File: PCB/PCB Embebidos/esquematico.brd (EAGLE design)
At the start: 91 x 70.9 mm, 30 parts, among them IC1 LM358N, IC2 317T, T1 BT138-V

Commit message: Estuve ruteando el PCB. Creo que esta terminado, pero tendria que revisarlo menos dormido
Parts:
- moved ALIMENTACION 39.9 mm to (6.96, 58.2), turned to 180 degrees
- moved CARGA 39.4 mm to (81.1, 24.6), turned to 270 degrees
- moved R9 17.7 mm to (13.7, 23.6), turned to 270 degrees
- moved R11 17.0 mm to (17.2, 20.8), turned to 270 degrees
- moved D1 16.2 mm to (72.2, 38.1), turned to 180 degrees
- moved IC2 15.4 mm to (-3.59, 25.9)
- moved R10 14.3 mm to (35.6, 62.5), turned to 0 degrees
- moved C1 14.3 mm to (7.43, 35.5)
- moved C4 13.6 mm to (7.37, 39.4)
- moved R2 13.2 mm to (65.1, 51.4)
- moved C5 9.36 mm to (12.9, 39.4)
- moved OK2 8.81 mm to (50.5, 37.1)
- moved R6 8.81 mm to (58.8, 37.1)
- moved OK3 8.62 mm to (59.9, 46.2)
- moved R5 8.37 mm to (42.7, 37.6), turned to 90 degrees
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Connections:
- net AC-: now also AC.2, CARGA.2; no longer CARGA.1
- net GND: now also ALIMENTACION.1, OK3.2; no longer ALIMENTACION.2
- net N$4: now also CARGA.1; no longer CARGA.2
- net VCC: now also ALIMENTACION.2; no longer ALIMENTACION.1
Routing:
- net VCC: track 0.00 -> 125.6 mm
- net AC+: track 0.00 -> 72.6 mm
- net AC-: track 0.00 -> 49.9 mm
- net N$4: track 0.00 -> 44.3 mm
- net VCC_5V: track 0.00 -> 32.6 mm
- net TERMOCUPLA: track 0.00 -> 31.8 mm
- net SAL_TERMOCUPLA: track 0.00 -> 30.6 mm
- net FASE: track 0.00 -> 28.4 mm
- net SAL_PT100: track 0.00 -> 25.6 mm
- net N$8: track 0.00 -> 25.3 mm
- net N$7: track 0.00 -> 18.6 mm
- net N$3: track 0.00 -> 13.6 mm
- net N$9: track 0.00 -> 13.0 mm
- net N$5: track 0.00 -> 12.1 mm
- net N$6: track 0.00 -> 11.9 mm
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- added copper zone on layer 16, net GND
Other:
- board size 91 x 70.9 mm -> 88.3 x 65.2 mm
- board text added: "Zorzuino ®"

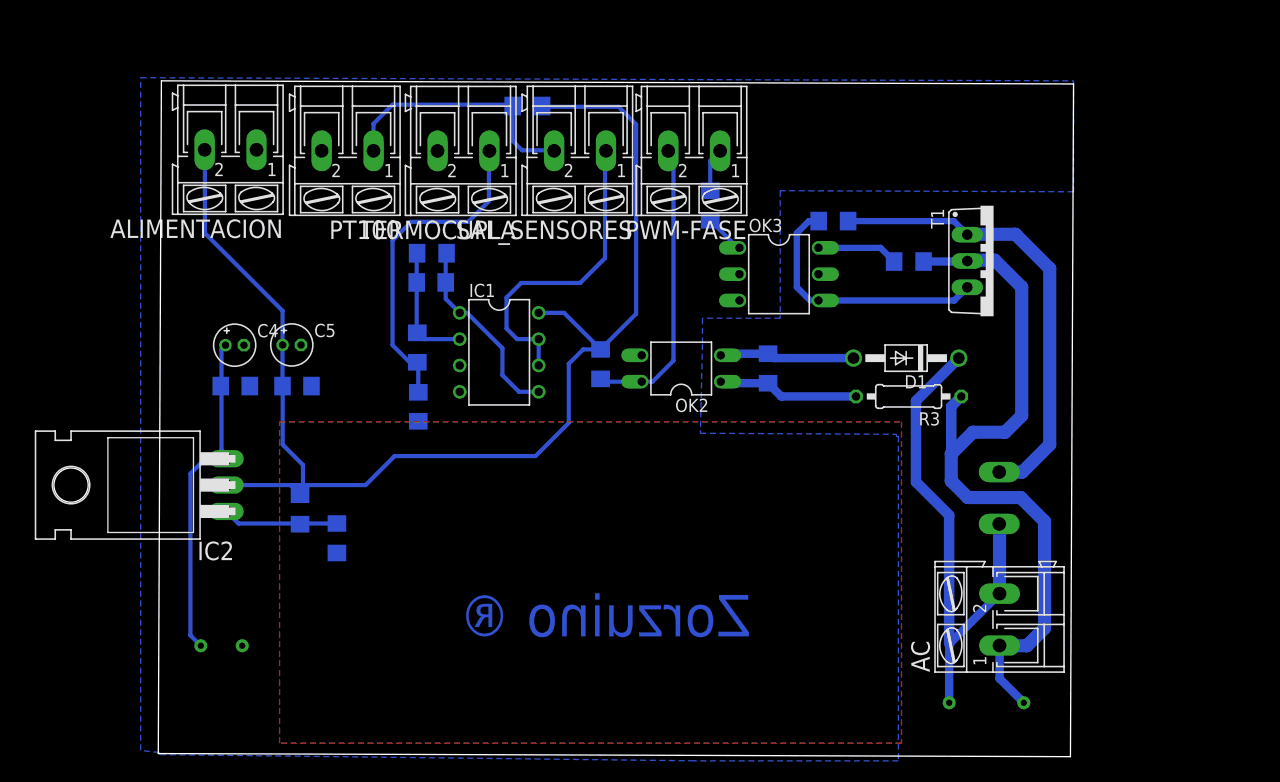
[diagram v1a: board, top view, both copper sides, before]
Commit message: Borre lo del PT100 y agrege las cosas para hacer el control del cooler. Falta ordenar un poco, ver si se puede achicar mas, y volver a rutear
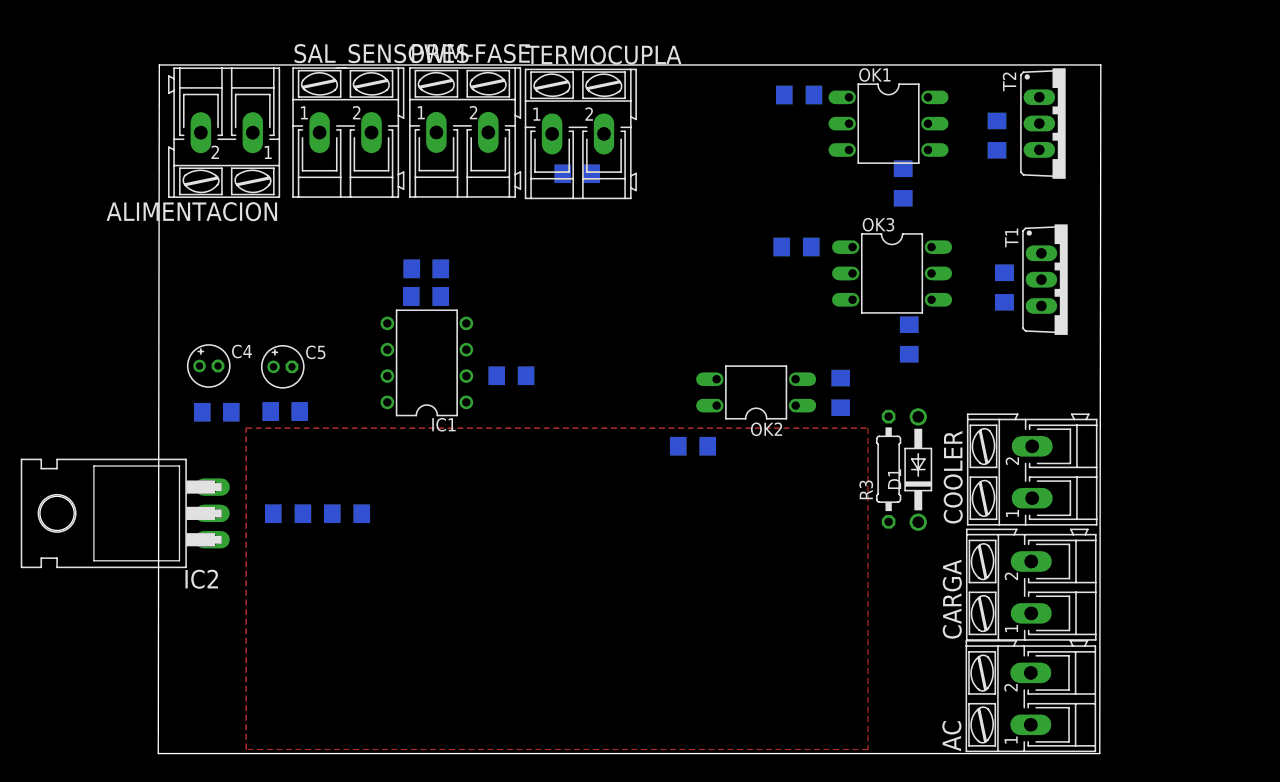
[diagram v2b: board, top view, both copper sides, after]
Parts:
- removed PT100: (no value), con-ptr500:AK300/2
- added COOLER: (no value), con-ptr500:AK300/2
- added OK1: MOC3031M, optocoupler:DIL06
- added R12, R13: 330, resistor:R1206
- added T2: BT138-V, triac:TO220BV
- R10: value 100 -> 680
- moved C6 27.2 mm to (40.4, 55.9), turned to 180 degrees
- moved R10 26.2 mm to (61.8, 63.5), turned to 180 degrees
- moved SAL_SENSORES 22.7 mm to (18.1, 59.9), turned to 0 degrees
- moved PWM-FASE 22.4 mm to (29.4, 59.9), turned to 0 degrees
- moved R2 17.7 mm to (81.6, 45.0), turned to 90 degrees
- moved R5 11.9 mm to (51.6, 29.6), turned to 0 degrees
- moved TERMOCUPLA 11.2 mm to (40.5, 59.8), turned to 0 degrees
- moved OK3 10.9 mm to (70.8, 46.3)
- moved D1 10.8 mm to (73.3, 27.4), turned to 90 degrees
- moved R8 9.47 mm to (34.1, 36.5), turned to 180 degrees
- moved R4 9.23 mm to (61.6, 48.9), turned to 180 degrees
- moved CARGA 9.14 mm to (84.2, 16.0), flipped to the top, turned to 90 degrees
- moved AC 8.22 mm to (84.2, 5.29)
- moved OK2 7.59 mm to (57.7, 34.8)
- moved R1 7.52 mm to (72.5, 40.0), turned to 270 degrees
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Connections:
- removed net SAL_PT100: PT100.1, R10.2, SAL_SENSORES.2
- new net COOLER_PIN: R10.1, SAL_SENSORES.2
- new net N$11: OK1.1, R10.2
- new net N$12: OK1.6, R12.1
- new net N$15: OK1.4, R13.1, T2.G
- new net N$17: COOLER.2, R13.2, T2.T1
- net AC+: now also R12.2, T2.T2
- net AC-: now also COOLER.1
- net GND: now also OK1.2; no longer PT100.2
- net VCC: no longer R10.1
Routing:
- net VCC: track 125.6 -> 0.00 mm
- net AC+: track 72.6 -> 0.00 mm, vias 1 -> 0
- net AC-: track 49.9 -> 0.00 mm, vias 1 -> 0
- net N$4: track 44.3 -> 0.00 mm
- net VCC_5V: track 32.6 -> 0.00 mm, vias 1 -> 0
- net TERMOCUPLA: track 31.8 -> 0.00 mm
- net SAL_TERMOCUPLA: track 30.6 -> 0.00 mm
- net FASE: track 28.4 -> 0.00 mm
- net SAL_PT100: track 25.6 -> 0.00 mm
- net N$8: track 25.3 -> 0.00 mm
- net N$7: track 18.6 -> 0.00 mm
- net N$3: track 13.6 -> 0.00 mm
- net N$9: track 13.0 -> 0.00 mm
- net N$5: track 12.1 -> 0.00 mm
- net N$6: track 11.9 -> 0.00 mm
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- removed copper zone on layer 16, net GND
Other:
- board size 88.3 x 65.2 mm -> 90.9 x 66.4 mm
- board text removed: "Zorzuino ®"

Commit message: El PCB esta listo para ser imprimido. Voy a comprar todos los componentes mañana y ya lo termino
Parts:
- moved R1 19.3 mm to (91.8, 39.5), turned to 180 degrees
- moved R12 15.4 mm to (87.3, 54.0), turned to 180 degrees
- moved COOLER 14.5 mm to (93.6, 16.0)
- moved CARGA 14.3 mm to (93.6, 26.9)
- moved PWM-FASE 14.2 mm to (43.5, 59.8), turned to 180 degrees
- moved OK3 11.1 mm to (81.9, 46.0)
- moved R13 11.1 mm to (92.0, 59.3)
- moved R2 11.1 mm to (92.7, 44.6)
- moved T1 11.1 mm to (98.8, 45.4)
- moved T2 11.1 mm to (98.6, 60.5)
- moved R5 10.3 mm to (61.9, 30.0)
- moved D1 9.47 mm to (82.8, 27.4)
- moved R3 9.47 mm to (79.9, 27.4)
- moved OK2 9.47 mm to (67.2, 34.8)
- moved AC 9.47 mm to (93.7, 5.29)
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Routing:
- net AC+: track 0.00 -> 134.3 mm, vias 0 -> 1
- net VCC: track 0.00 -> 101.5 mm
- net N$17: track 0.00 -> 80.1 mm
- net AC-: track 0.00 -> 63.0 mm, vias 0 -> 1
- net FASE: track 0.00 -> 51.2 mm
- net N$4: track 0.00 -> 50.3 mm
- net COOLER_PIN: track 0.00 -> 38.5 mm
- net VCC_5V: track 0.00 -> 27.0 mm, vias 0 -> 1
- net TERMOCUPLA: track 0.00 -> 25.4 mm
- net SAL_TERMOCUPLA: track 0.00 -> 24.1 mm
- net PWM: track 0.00 -> 23.6 mm
- net N$15: track 0.00 -> 17.3 mm
- net N$7: track 0.00 -> 17.0 mm
- net N$12: track 0.00 -> 16.1 mm
- net N$1: track 0.00 -> 15.8 mm, vias 0 -> 2
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- added copper zone on layer 16, net GND
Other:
- board size 90.9 x 66.4 mm -> 105.1 x 66.5 mm
- board text added: "Zorzuino ®"

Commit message: Movi unas cosas para que entren mejor los disipadores
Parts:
- moved C1 10.3 mm to (5.74, 43.2)
- moved C2 10.3 mm to (12.3, 43.2)
- moved C4 10.3 mm to (4.96, 47.6)
- moved C5 10.3 mm to (12.1, 47.6)
- moved IC2 10.3 mm to (-4.85, 33.4)
- moved R9 10.3 mm to (12.6, 33.4)
- moved R11 8.89 mm to (16.9, 31.9), turned to 270 degrees
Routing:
- net VCC: track 101.5 -> 86.7 mm
- net VCC_5V: track 27.0 -> 37.2 mm

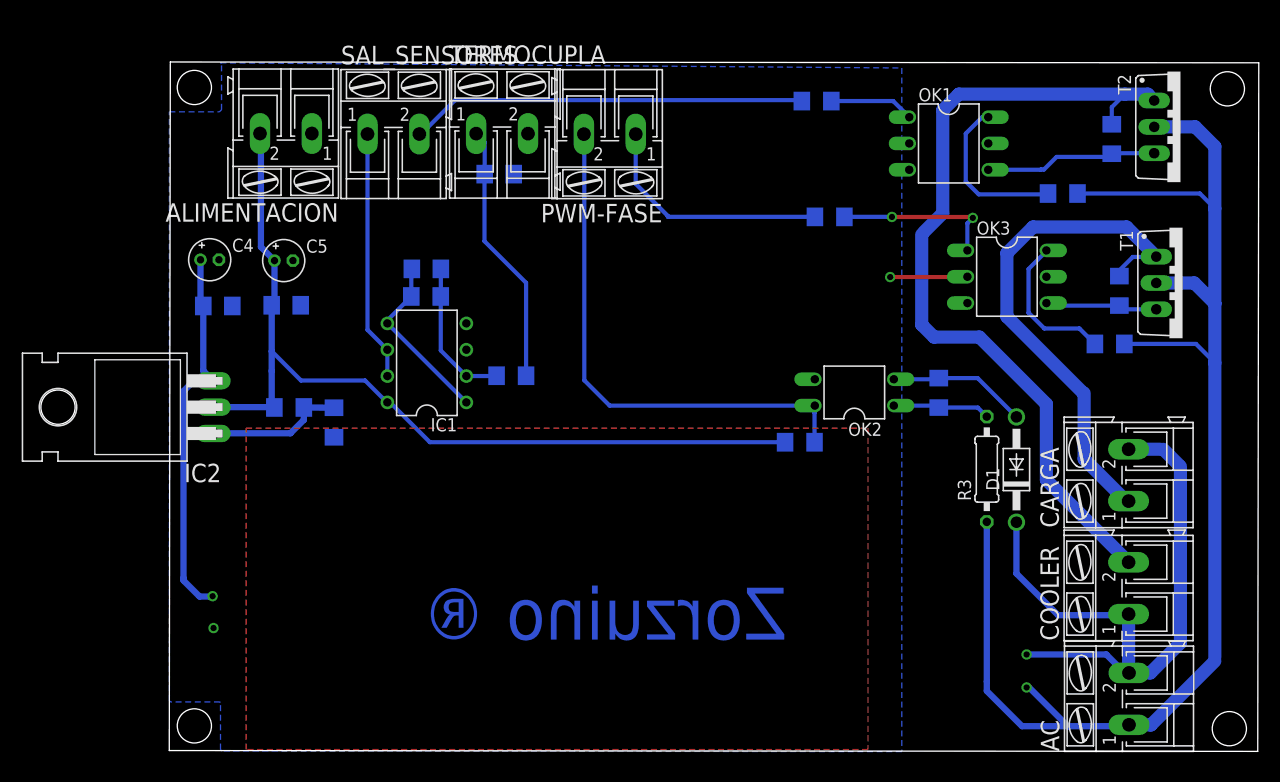
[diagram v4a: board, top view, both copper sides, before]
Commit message: Tuve que rehacer la placa porque habian quedado muy finas las pistas. El codigo no lo modifique, y parece estar andando todo bien. Mañana le voy a poner disipadores a los triacs y voy a empezar a poner las curvas de referencia
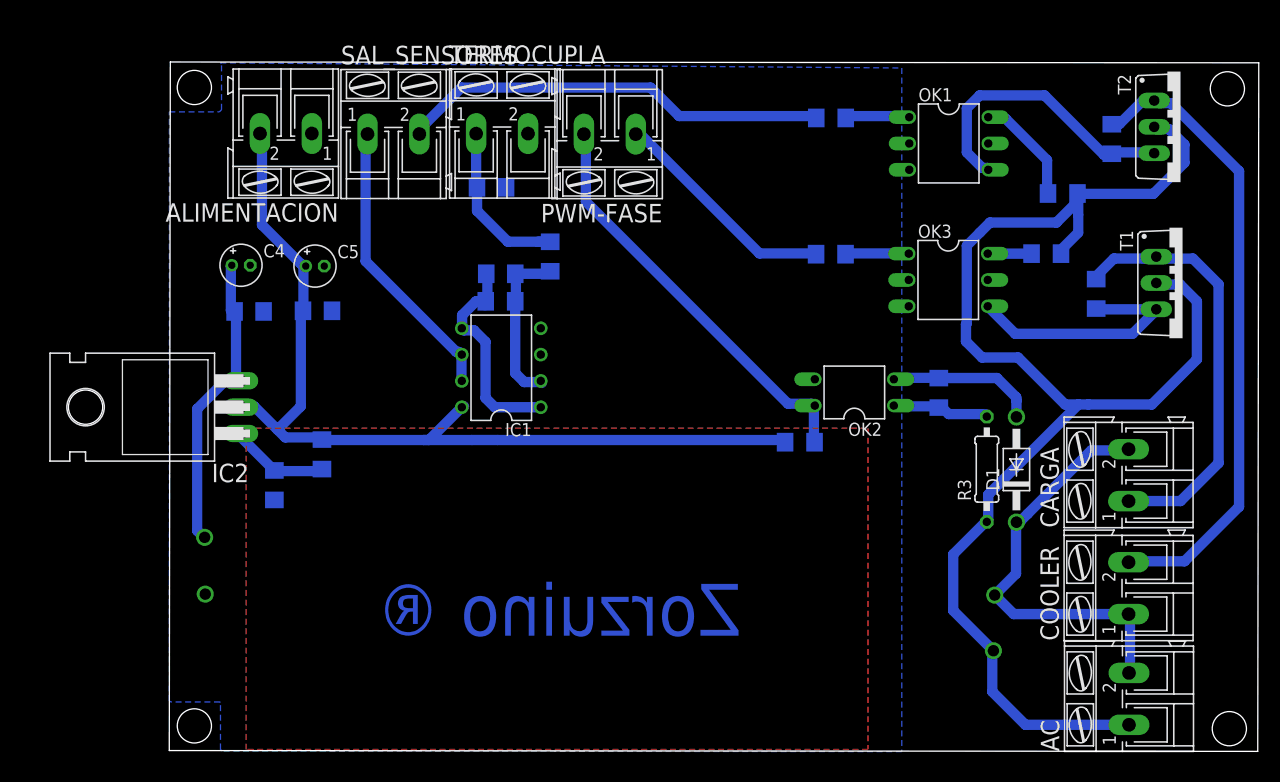
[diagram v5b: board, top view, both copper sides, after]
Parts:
- R1, R12, R13, R2: value 330 -> 560
- R3: value 20k -> 100k
- moved R8 12.1 mm to (37.8, 48.0), turned to 90 degrees
- moved R1 10.6 mm to (85.7, 48.2)
- moved R11 8.35 mm to (11.2, 25.9)
- moved IC1 7.20 mm to (33.1, 37.2)
- moved C3 7.20 mm to (33.0, 46.3)
- moved R7 7.20 mm to (33.0, 43.6)
- moved OK3 5.67 mm to (76.2, 45.7)
- moved R9 5.52 mm to (15.8, 28.9), turned to 270 degrees
- moved R4 3.60 mm to (64.9, 48.2)
- moved C4 3.07 mm to (7.98, 47.1)
- moved C1 3.07 mm to (8.76, 42.6)
- moved C2 3.07 mm to (15.4, 42.7)
- moved C5 3.07 mm to (15.1, 47.0)
- moved IC2 2.66 mm to (-2.19, 33.4)
- moved R2 2.26 mm to (90.5, 44.4)
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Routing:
- net AC-: track 63.0 -> 41.5 mm
- net N$17: track 80.1 -> 61.3 mm
- net N$8: track 10.8 -> 24.4 mm
- net N$15: track 17.3 -> 28.2 mm
- net FASE: track 51.2 -> 40.5 mm
- net N$2: track 14.4 -> 4.23 mm
- net N$1: track 15.8 -> 6.11 mm, vias 2 -> 0
- net TERMOCUPLA: track 25.4 -> 17.1 mm
- net GND: track 7.46 -> 0.00 mm, vias 2 -> 1
- net N$4: track 50.3 -> 42.8 mm
- net VCC_5V: track 37.2 -> 29.9 mm
- net N$12: track 16.1 -> 10.6 mm
- net N$7: track 17.0 -> 21.4 mm
- net VCC: track 86.7 -> 91.0 mm
- net SAL_TERMOCUPLA: track 24.1 -> 28.0 mm
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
